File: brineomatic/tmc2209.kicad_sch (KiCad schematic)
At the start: 18 parts, among them J21 Conn_01x04, U9 TMC2209-LA

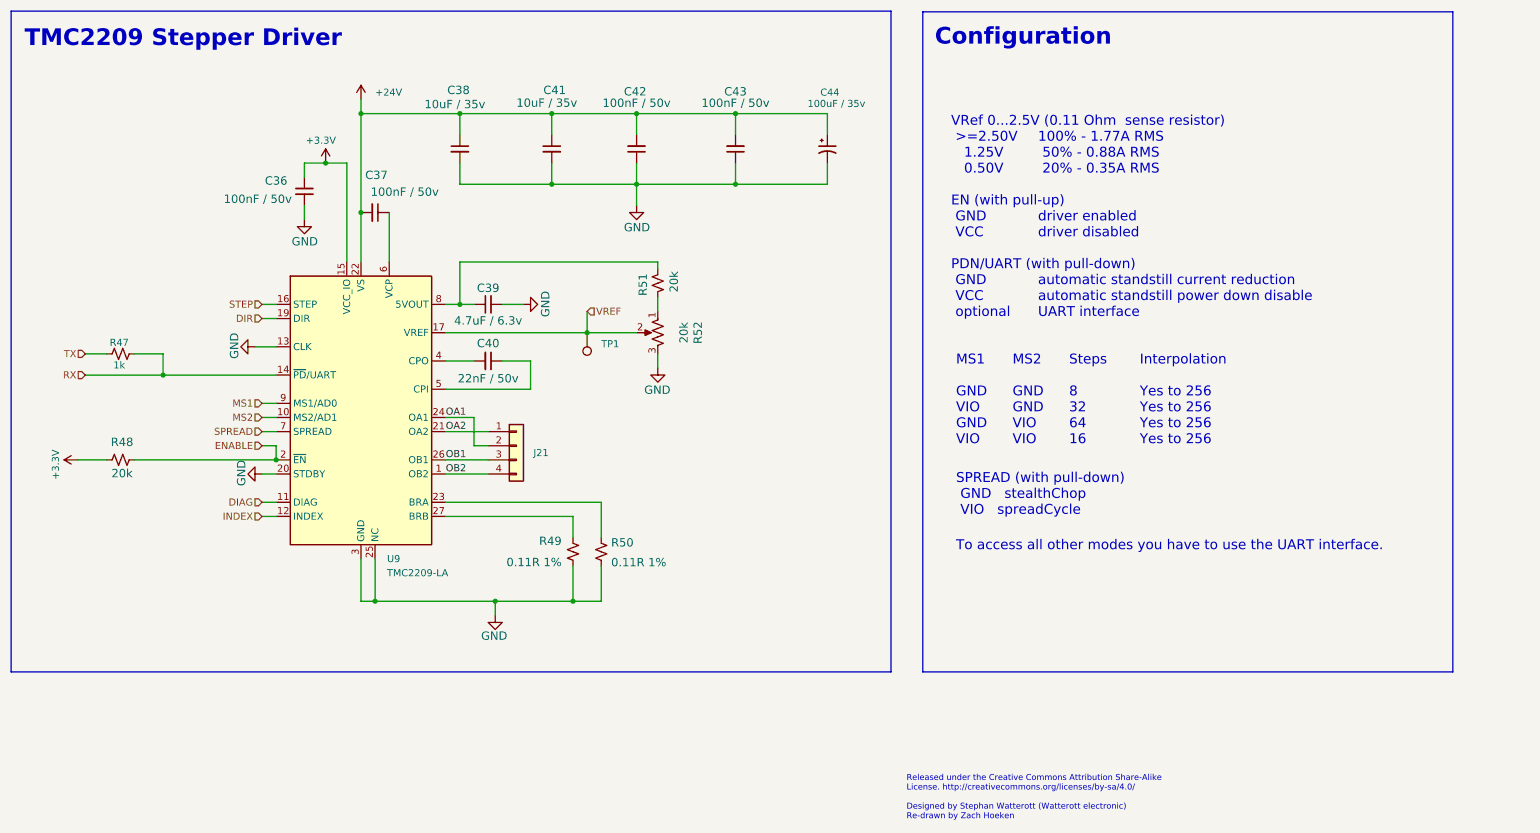
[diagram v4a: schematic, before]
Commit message: stacked tds, removed stepper vref, pulled in esp32-s3 schematic, added extra relay output
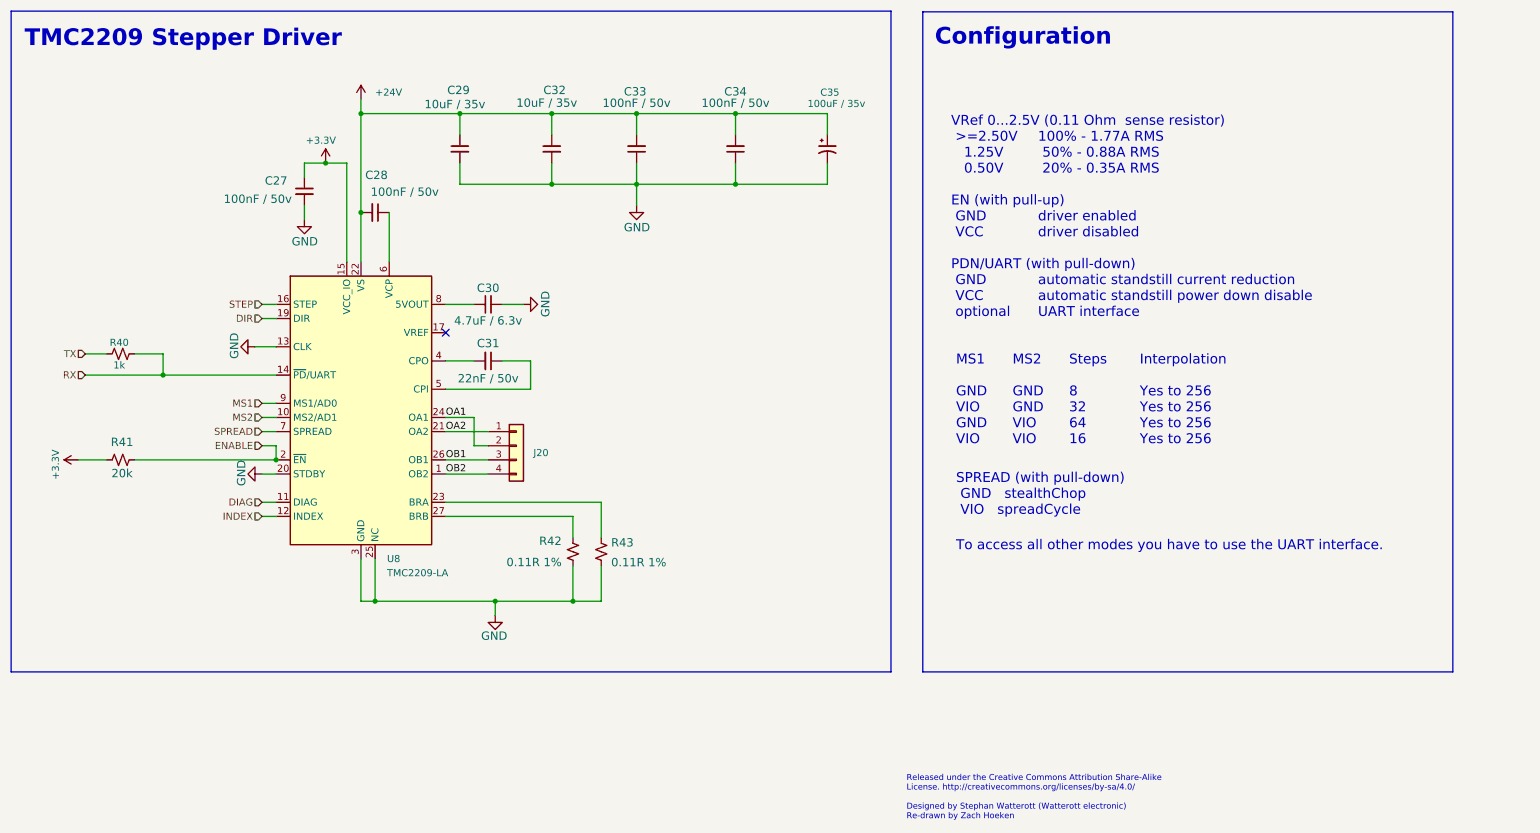
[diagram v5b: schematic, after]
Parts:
- removed R51: 20k, Resistor_SMD:R_0603_1608Metric, symbol Device:R_Small_US
- removed R52: 20k, Potentiometer_SMD:Potentiometer_Bourns_TC33X_Vertical, symbol Device:R_Potentiometer_US
- removed TP1: TestPoint, TestPoint:TestPoint_THTPad_D3.0mm_Drill1.5mm, symbol Connector:TestPoint
- renumbered C36 to C27, C37 to C28, C38 to C29, C39 to C30, C40 to C31, C41 to C32, C42 to C33, C43 to C34, C44 to C35, J21 to J20, R47 to R40, R48 to R41, R49 to R42, R50 to R43, U9 to U8
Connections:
- net VREF: no longer names the net of U8.17 (VREF)
- no-connect marks 0 -> 1

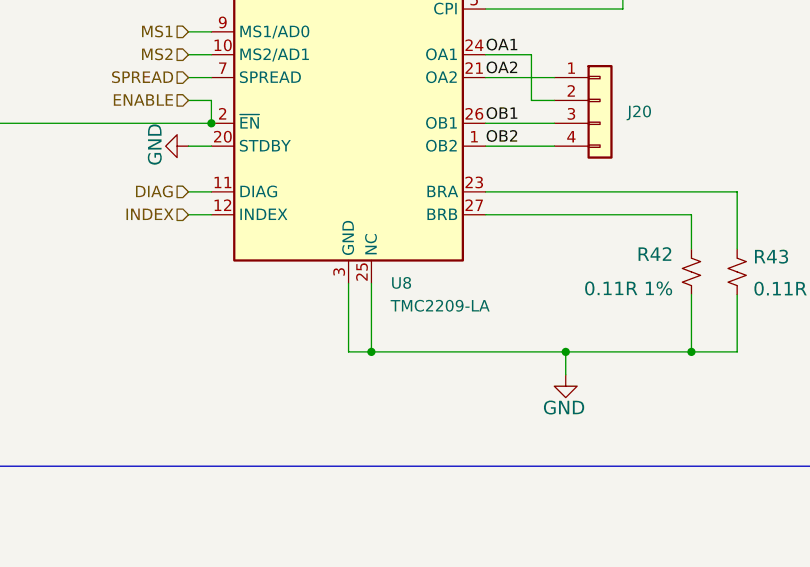
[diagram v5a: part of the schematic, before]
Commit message: all connectors are now flush withe 3mm outside edge of the case
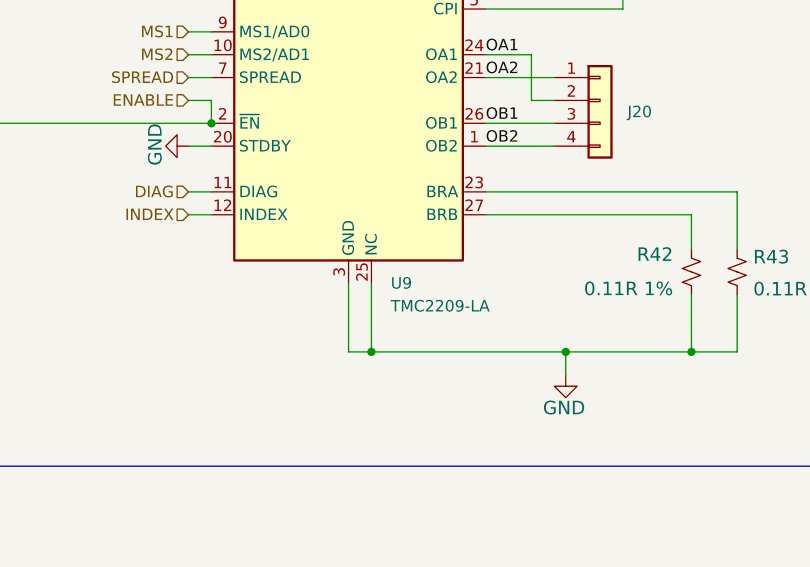
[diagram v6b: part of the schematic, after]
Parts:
- renumbered U8 to U9
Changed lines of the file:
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@@
 		(dnp no)
 		(fields_autoplaced yes)
-		(property "Reference" "U8"
+		(property "Reference" "U9"
 			(at 85.9633 130.81 0)
 			(effects
@@
 			(project ""
 				(path "/96477ae2-ef08-48f3-8dd4-fe4478541f68/0f01c39f-0c25-414e-9ed3-1ba09e2af0c5"
-					(reference "U8")
+					(reference "U9")
 					(unit 1)
 				)

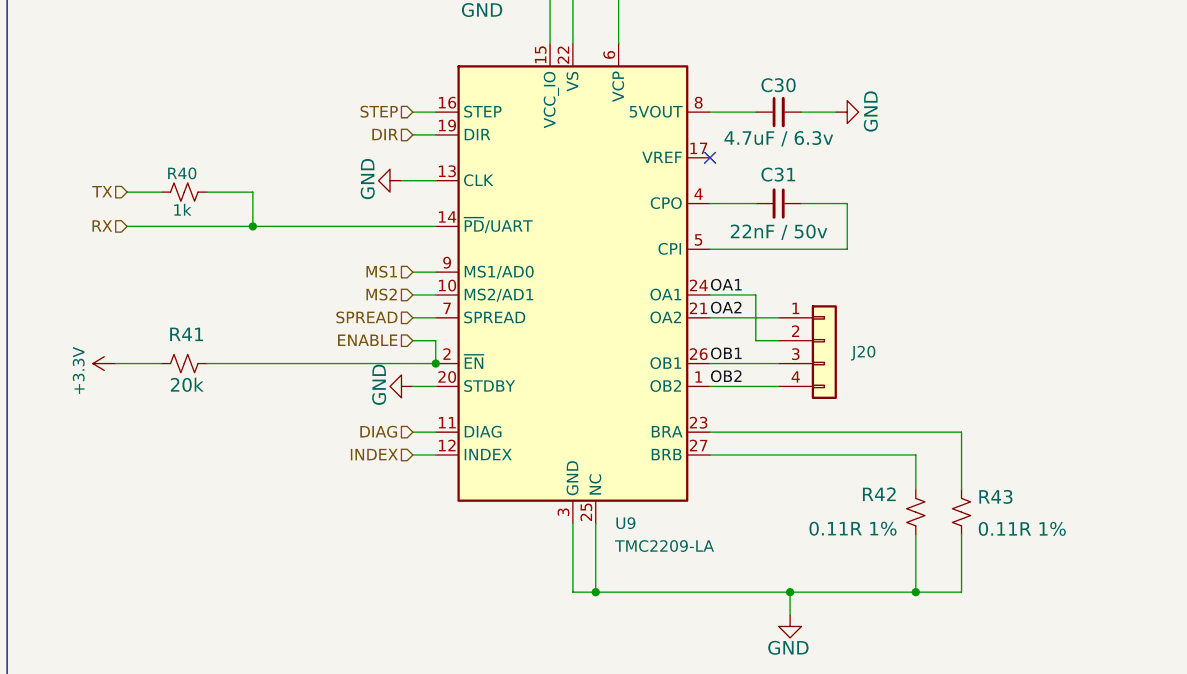
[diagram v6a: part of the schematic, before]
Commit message: schematic tidy, usb c position verified, component placement work.
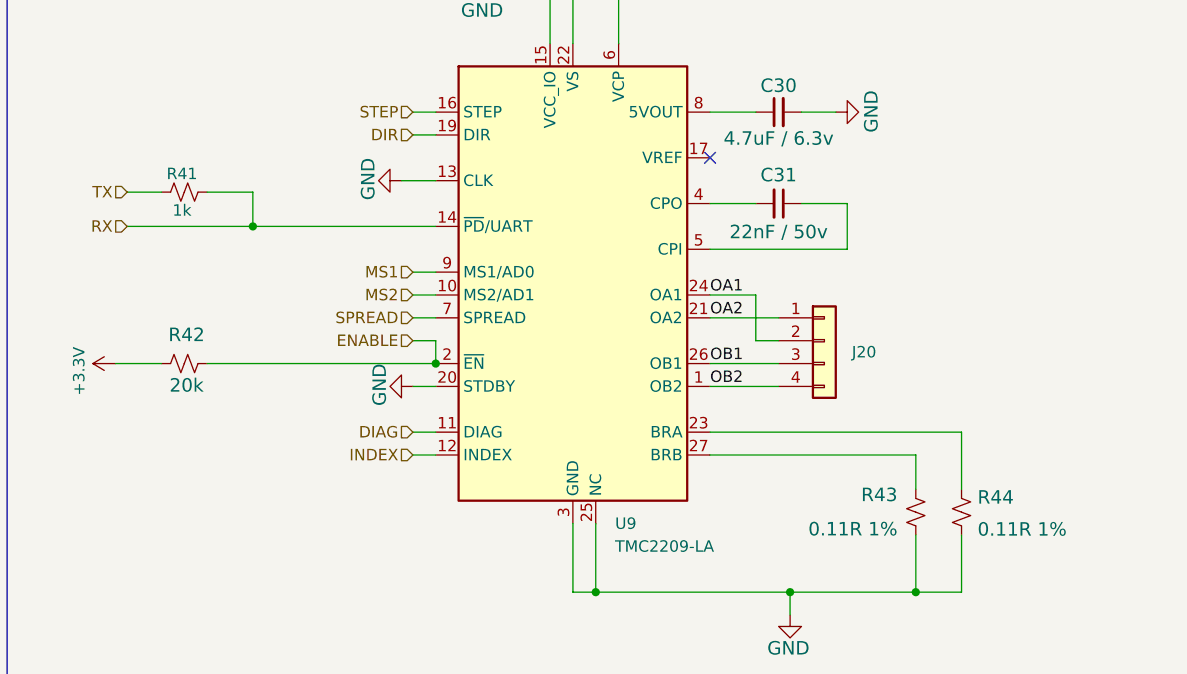
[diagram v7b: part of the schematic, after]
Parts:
- renumbered R40 to R41, R41 to R42, R42 to R43, R43 to R44
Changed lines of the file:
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@@
 		(on_board yes)
 		(dnp no)
-		(property "Reference" "R41"
+		(property "Reference" "R42"
 			(at 38.354 108.966 90)
 			(effects
@@
 			(project "brineomatic"
 				(path "/96477ae2-ef08-48f3-8dd4-fe4478541f68/0f01c39f-0c25-414e-9ed3-1ba09e2af0c5"
-					(reference "R41")
+					(reference "R42")
 					(unit 1)
 				)
@@
 		(on_board yes)
 		(dnp no)
-		(property "Reference" "R43"
+		(property "Reference" "R44"
 			(at 126.238 128.778 0)
 			(effects
@@
 			(project "brineomatic"
 				(path "/96477ae2-ef08-48f3-8dd4-fe4478541f68/0f01c39f-0c25-414e-9ed3-1ba09e2af0c5"
-					(reference "R43")
+					(reference "R44")
 					(unit 1)
 				)
@@
 		(on_board yes)
 		(dnp no)
-		(property "Reference" "R40"
+		(property "Reference" "R41"
 			(at 37.846 91.948 90)
 			(effects
@@
 			(project "brineomatic"
 				(path "/96477ae2-ef08-48f3-8dd4-fe4478541f68/0f01c39f-0c25-414e-9ed3-1ba09e2af0c5"
-					(reference "R40")
+					(reference "R41")
 					(unit 1)
 				)
@@
 		(on_board yes)
 		(dnp no)
-		(property "Reference" "#PWR061"
+		(property "Reference" "#PWR063"
 			(at 74.93 63.5 0)
 			(effects
@@
 			(project "brineomatic"
 				(path "/96477ae2-ef08-48f3-8dd4-fe4478541f68/0f01c39f-0c25-414e-9ed3-1ba09e2af0c5"
-					(reference "#PWR061")
+					(reference "#PWR063")
 					(unit 1)
 				)
@@
 		(on_board yes)
 		(dnp no)
-		(property "Reference" "R42"
+		(property "Reference" "R43"
 			(at 117.348 126.746 0)
 			(effects
@@
 			(project "brineomatic"
 				(path "/96477ae2-ef08-48f3-8dd4-fe4478541f68/0f01c39f-0c25-414e-9ed3-1ba09e2af0c5"
-					(reference "R42")
+					(reference "R43")
 					(unit 1)
 				)
@@
 		(on_board yes)
 		(dnp no)
-		(property "Reference" "#PWR060"
+		(property "Reference" "#PWR062"
 			(at 34.29 113.03 0)
 			(effects
@@
 			(project "brineomatic"
 				(path "/96477ae2-ef08-48f3-8dd4-fe4478541f68/0f01c39f-0c25-414e-9ed3-1ba09e2af0c5"
-					(reference "#PWR060")
+					(reference "#PWR062")
 					(unit 1)
 				)
@@
 		(dnp no)
 		(fields_autoplaced yes)
-		(property "Reference" "#PWR062"
+		(property "Reference" "#PWR064"
 			(at 81.28 52.07 0)
 			(effects
@@
 			(project ""
 				(path "/96477ae2-ef08-48f3-8dd4-fe4478541f68/0f01c39f-0c25-414e-9ed3-1ba09e2af0c5"
-					(reference "#PWR062")
-					(unit 1)
-				)
+					(reference "#PWR064")
+					(unit 1)
+				)

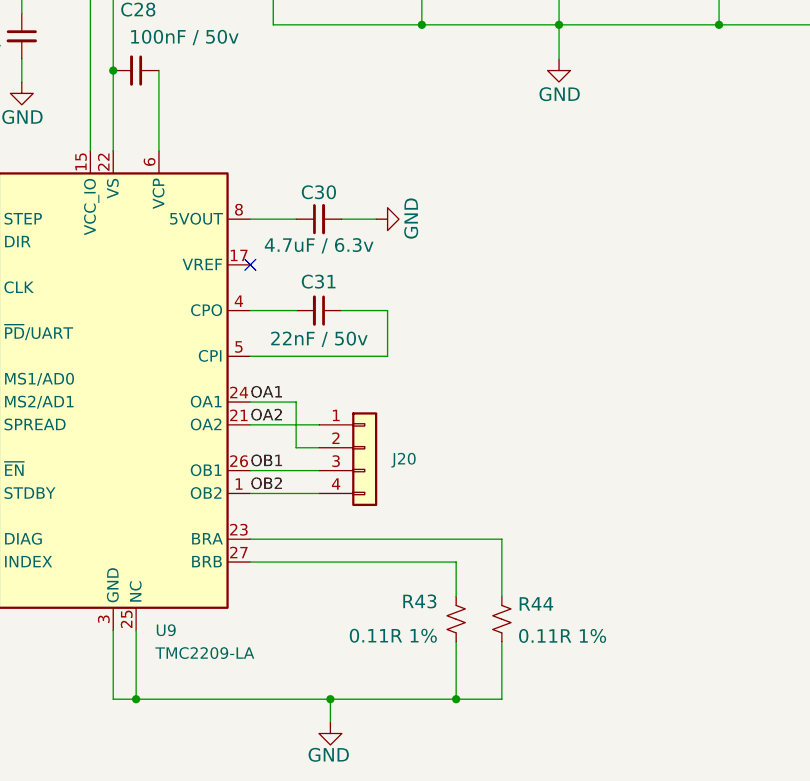
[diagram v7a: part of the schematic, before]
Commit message: added voltage divider to vref.  more component shuffling.
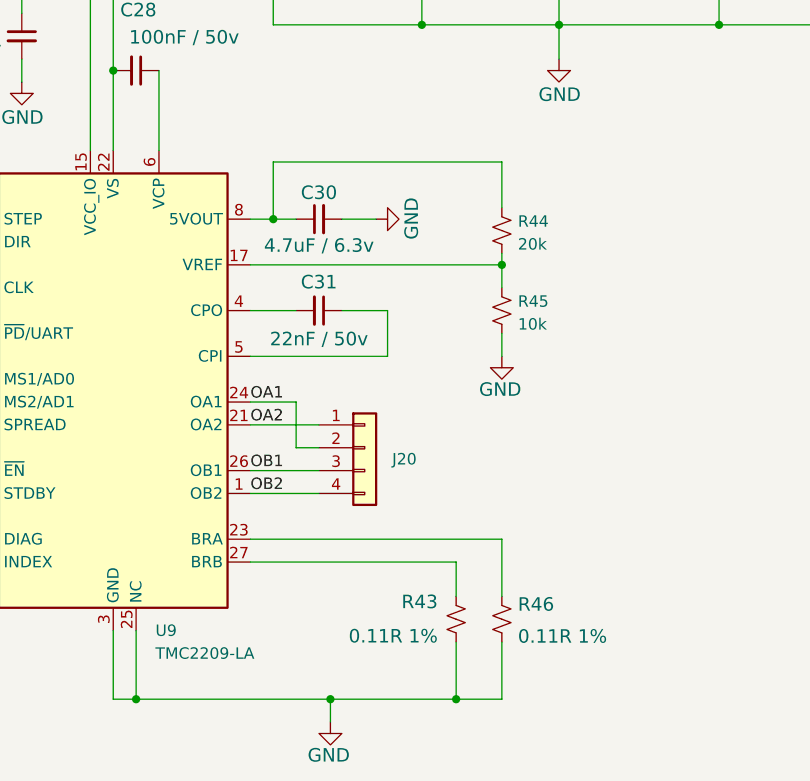
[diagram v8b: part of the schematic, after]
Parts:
- added R44: 20k, Resistor_SMD:R_0603_1608Metric, symbol Device:R_Small_US
- added R45: 10k, Resistor_SMD:R_0603_1608Metric, symbol Device:R_Small_US
- renumbered R44 to R46
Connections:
- net GND: now also R45.1
- net at U9.17 (VREF): now also R44.1, R45.2
- net at C30.1, U9.8 (5VOUT): now also R44.2
- no-connect marks 1 -> 0
